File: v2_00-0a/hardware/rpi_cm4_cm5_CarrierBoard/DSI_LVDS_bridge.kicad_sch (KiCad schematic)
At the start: 28 parts, among them Q10 SSM3K56FS,LF, Q11 SSM3K56FS,LF, U15 SN65DSI84ZXHR, U16 SN74LVC1G125DBVR

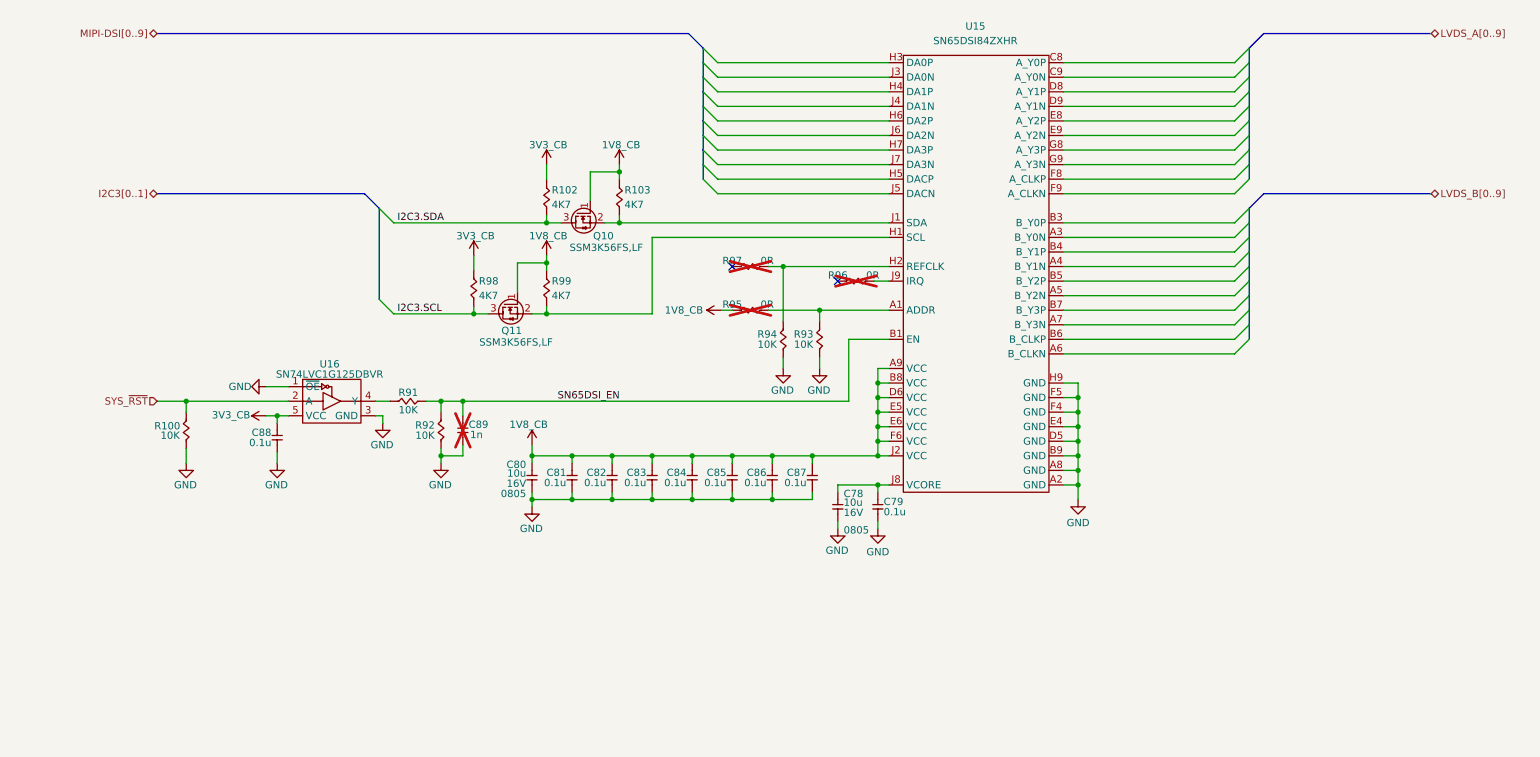
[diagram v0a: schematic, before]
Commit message: Add new page and update schematics
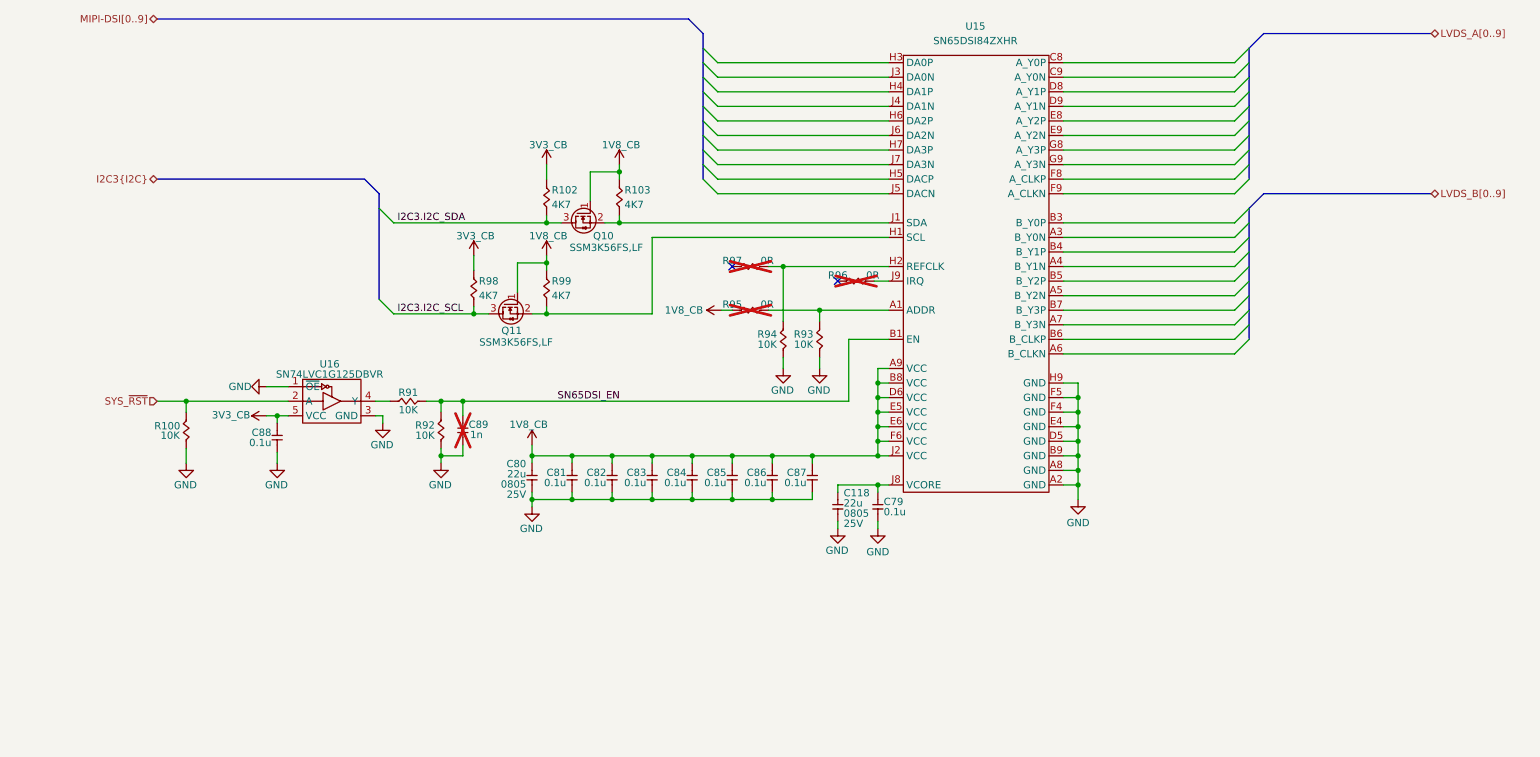
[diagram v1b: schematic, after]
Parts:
- removed C78, C80: 10u, footprint:CAP_NONPOL_0805, symbol KicadCompDb:Capacitors/CAP_CER_SMT_00004
- added C118, C80: 22u, footprint:CAP_NONPOL_0805, symbol KicadCompDb:Capacitors/CAP_CER_SMT_00011
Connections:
- net 1V8_CB: now also C80.2
- net GND: now also C118.1, C80.1
- net at C79.2, U15.J8 (VCORE): now also C118.2
- net I2C3.SCL renamed I2C3.I2C_SCL
- net I2C3.SDA renamed I2C3.I2C_SDA

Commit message: Add design notes (power table) and latest changes to power supply and power input
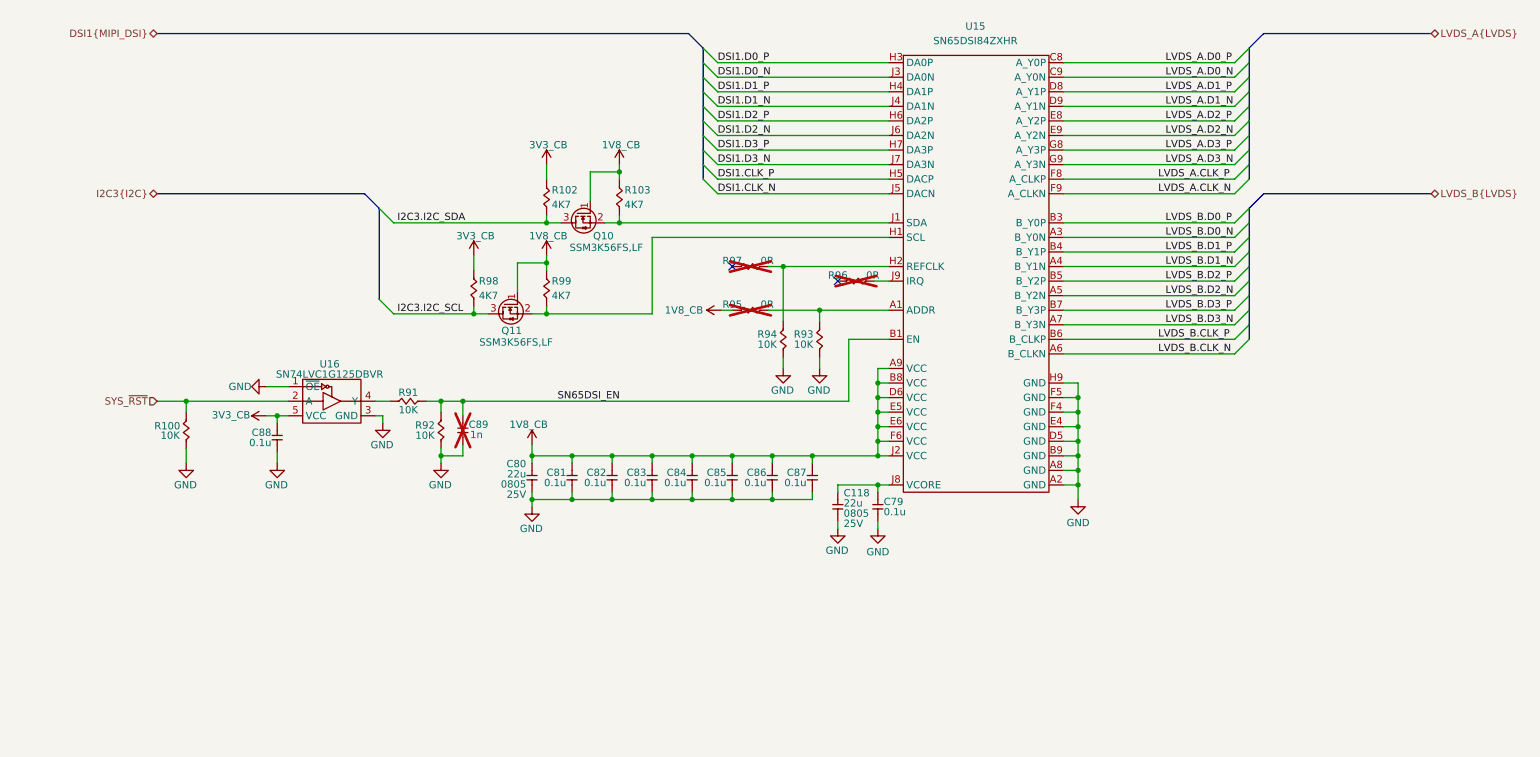
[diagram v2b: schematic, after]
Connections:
- net LVDS_B.D0_N: now reaches U15.A3 (B_Y0N)
- net LVDS_B.D1_N: now reaches U15.A4 (B_Y1N)
- net LVDS_B.D2_N: now reaches U15.A5 (B_Y2N)
- net LVDS_B.CLK_N: now reaches U15.A6 (B_CLKN)
- net LVDS_B.D3_N: now reaches U15.A7 (B_Y3N)
- net LVDS_B.D0_P: now reaches U15.B3 (B_Y0P)
- net LVDS_B.D1_P: now reaches U15.B4 (B_Y1P)
- net LVDS_B.D2_P: now reaches U15.B5 (B_Y2P)
- net LVDS_B.CLK_P: now reaches U15.B6 (B_CLKP)
- net LVDS_B.D3_P: now reaches U15.B7 (B_Y3P)
- net LVDS_A.D0_P: now reaches U15.C8 (A_Y0P)
- net LVDS_A.D0_N: now reaches U15.C9 (A_Y0N)
- net LVDS_A.D1_P: now reaches U15.D8 (A_Y1P)
- net LVDS_A.D1_N: now reaches U15.D9 (A_Y1N)
- net LVDS_A.D2_P: now reaches U15.E8 (A_Y2P)
- net LVDS_A.D2_N: now reaches U15.E9 (A_Y2N)
- net LVDS_A.CLK_P: now reaches U15.F8 (A_CLKP)
- net LVDS_A.CLK_N: now reaches U15.F9 (A_CLKN)
- net LVDS_A.D3_P: now reaches U15.G8 (A_Y3P)
- net LVDS_A.D3_N: now reaches U15.G9 (A_Y3N)
- net DSI1.D0_P: now reaches U15.H3 (DA0P)
- net DSI1.D1_P: now reaches U15.H4 (DA1P)
- net DSI1.CLK_P: now reaches U15.H5 (DACP)
- net DSI1.D2_P: now reaches U15.H6 (DA2P)
- net DSI1.D3_P: now reaches U15.H7 (DA3P)
- net DSI1.D0_N: now reaches U15.J3 (DA0N)
- net DSI1.D1_N: now reaches U15.J4 (DA1N)
- net DSI1.CLK_N: now reaches U15.J5 (DACN)
- net DSI1.D2_N: now reaches U15.J6 (DA2N)
- net DSI1.D3_N: now reaches U15.J7 (DA3N)

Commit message: Update schematic
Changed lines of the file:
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@@
 	)
 	(hierarchical_label "LVDS_A{LVDS}"
-		(shape bidirectional)
+		(shape output)
 		(at 260.35 48.895 0)
 		(effects
@@
 	)
 	(hierarchical_label "LVDS_B{LVDS}"
-		(shape bidirectional)
+		(shape output)
 		(at 260.35 76.835 0)
 		(effects

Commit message: Add and modify existing schematics
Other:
- note added: "Resistors are 1% 1/16W 0402 unless otherwise noted Capacitors are 10% 50V X7R 0402 unless otherwise noted"
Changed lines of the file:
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@@
+		)
+	)
+	(text "Resistors are 1% 1/16W 0402 unless otherwise noted\nCapacitors are 10% 50V X7R 0402 unless otherwise noted"
+		(exclude_from_sim no)
+		(at 12.7 170.942 0)
+		(effects
+			(font
+				(size 1.27 1.27)
+			)
+			(justify left)
 		)
 	)
